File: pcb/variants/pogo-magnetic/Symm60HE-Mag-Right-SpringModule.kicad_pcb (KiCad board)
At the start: 2 copper layers, 32 x 18 mm, 2 parts

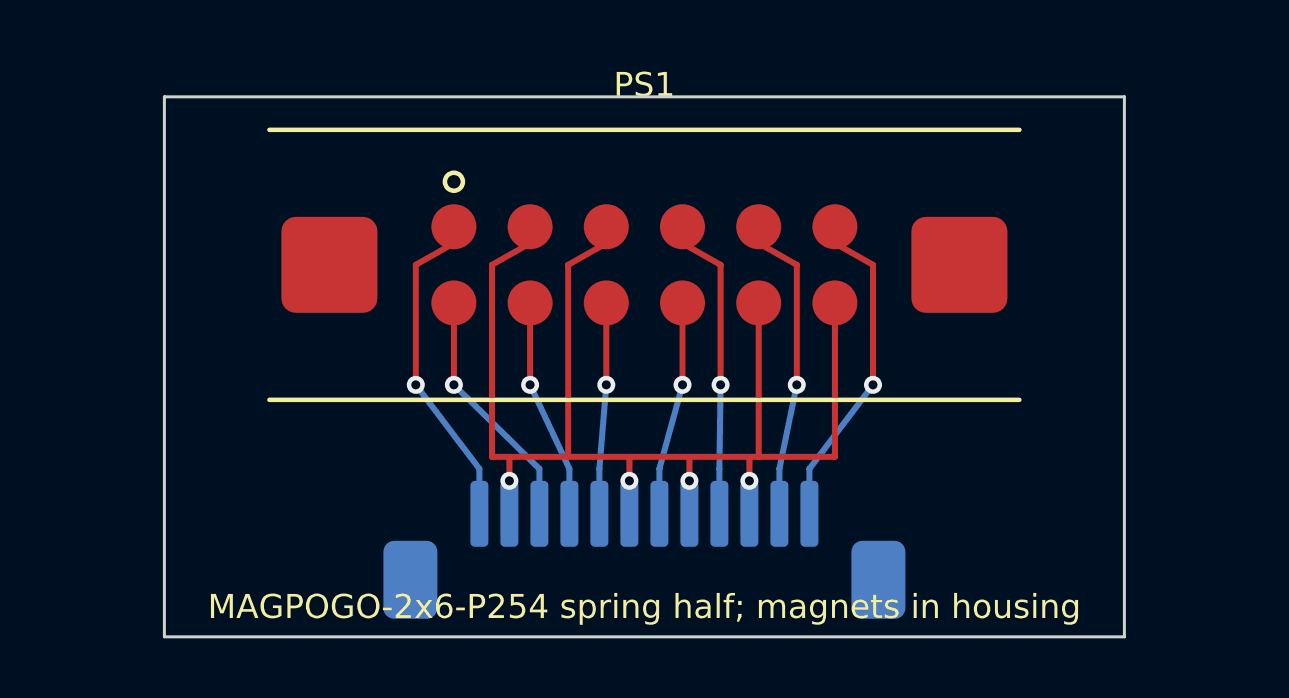
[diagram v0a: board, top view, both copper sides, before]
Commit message: Survey the stocked magnetic pogo parts at twelve contacts and up
No manufacturer catalogue publishes a magnetic part above eight contacts, but
the ODM market does: single row on 2.54 mm goes to twenty, and dual row on
2.54 mm offers 8, 10, 12, 14 and 20 poles. Record the families with their
contact spans, since span is what decides whether a part fits the kernel.

A single-row twelve-contact part spans 27.94 mm, so about a 40 mm housing on a
47 mm module. The 2 x 6 dual row spans 12.70 mm on the 32 mm module this
variant already builds, which is why it wins despite the harder fanout.

Sixteen was tried: PER_ROW = 8 generates and routes but leaves three clearance
flags on the left half instead of two, so the crossing is the anchor geometry
rather than a shortage of slots, and it costs 5 mm of module length for four
spare grounds. Reverted to twelve.

Also move footprint generation into tools/make_mag_pogo_footprints.py so the
ICD constants drive the land pattern, and generalise the verifier's ground
count so either width checks.

Co-Authored-By: Claude Opus 5 <noreply@anthropic.com>
Claude-Session: https://claude.ai/code/session_01CRkZ4zVz5Mq7Fa3C5HAmii
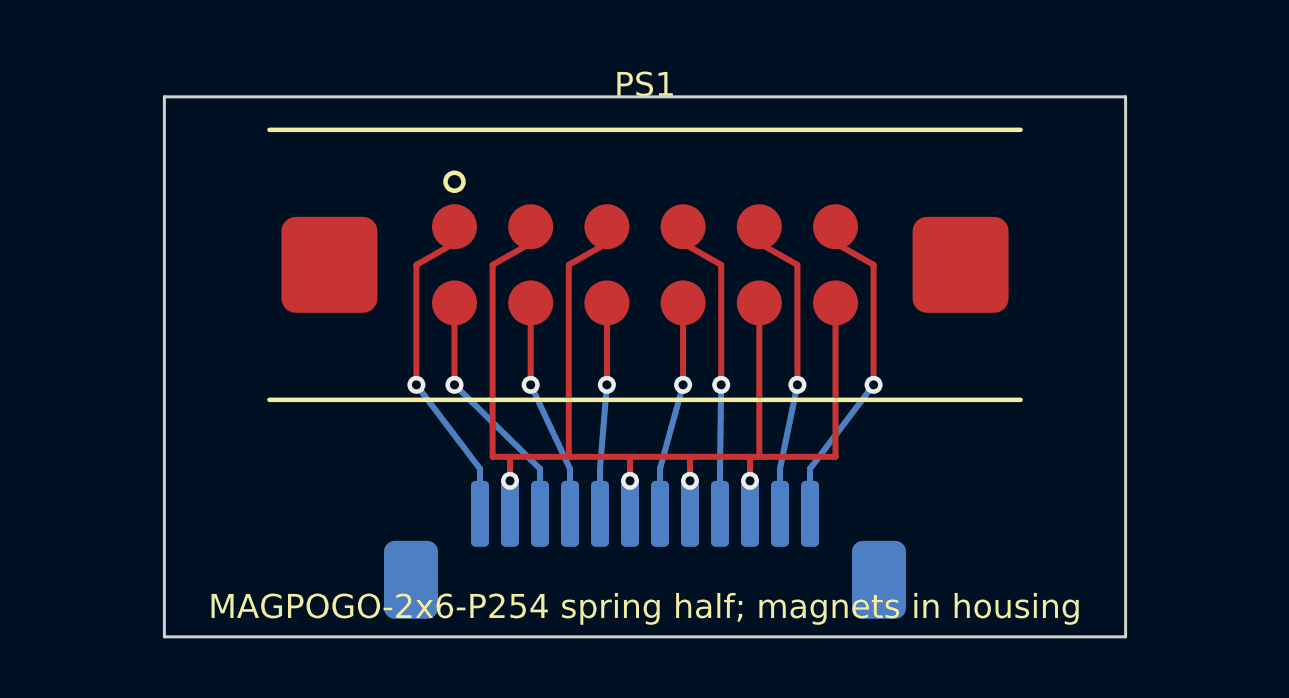
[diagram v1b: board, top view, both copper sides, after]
